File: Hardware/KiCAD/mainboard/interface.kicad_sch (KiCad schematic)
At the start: 22 parts, among them J2 USB_C, J3 UART, J4 Conn_01x30, J5 STLink, Q1 BSS138, U5 USBLC6-2

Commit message: Add files via upload
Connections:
- net BTN_F1: now also J4.18 (Pin_18)
- net GND: now also J4.10 (Pin_10), J4.26 (Pin_26), J4.28 (Pin_28)
- net VDD: now also J4.1 (Pin_1), J4.16 (Pin_16), J4.17 (Pin_17)
- net OLED_SPI_MOSI: now reaches J4.11 (Pin_11)
- net OLED_SPI_SCK: now reaches J4.12 (Pin_12)
- net OLED_CS: now reaches J4.13 (Pin_13)
- net OLED_DC: now reaches J4.14 (Pin_14)
- net OLED_RST: now reaches J4.15 (Pin_15)
- net BTN_F2: now reaches J4.19 (Pin_19)
- net C4: now reaches J4.2 (Pin_2)
- net PTT_IN: now reaches J4.20 (Pin_20)
- net ENC_A: now reaches J4.21 (Pin_21)
- net ENC_B: now reaches J4.22 (Pin_22)
- net ENC_BTN: now reaches J4.23 (Pin_23)
- net MIC_MUTE: now reaches J4.24 (Pin_24)
- net MIC_GAIN: now reaches J4.25 (Pin_25)
- net AUDIO_MIC: now reaches J4.27 (Pin_27)
- net SPK_P: now reaches J4.29 (Pin_29)
- net C3: now reaches J4.3 (Pin_3)
- net SPK_N: now reaches J4.30 (Pin_30)
- net C2: now reaches J4.4 (Pin_4)
- net C1: now reaches J4.5 (Pin_5)
- net R4: now reaches J4.6 (Pin_6)
- net R3: now reaches J4.7 (Pin_7)
- net R2: now reaches J4.8 (Pin_8)
- net R1: now reaches J4.9 (Pin_9)
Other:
- note removed: "TODO"
- moved on the sheet: J4

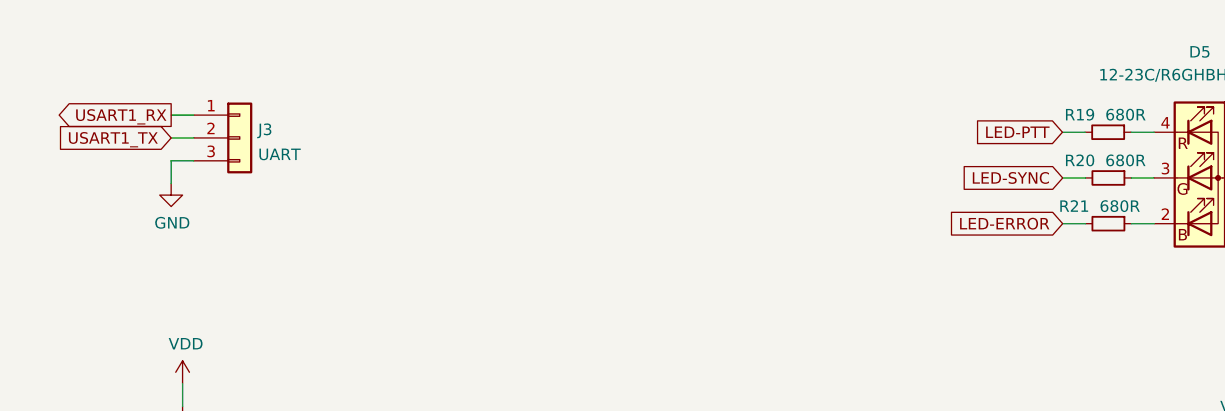
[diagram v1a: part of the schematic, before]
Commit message: J3 UART conn change
Fixes #33
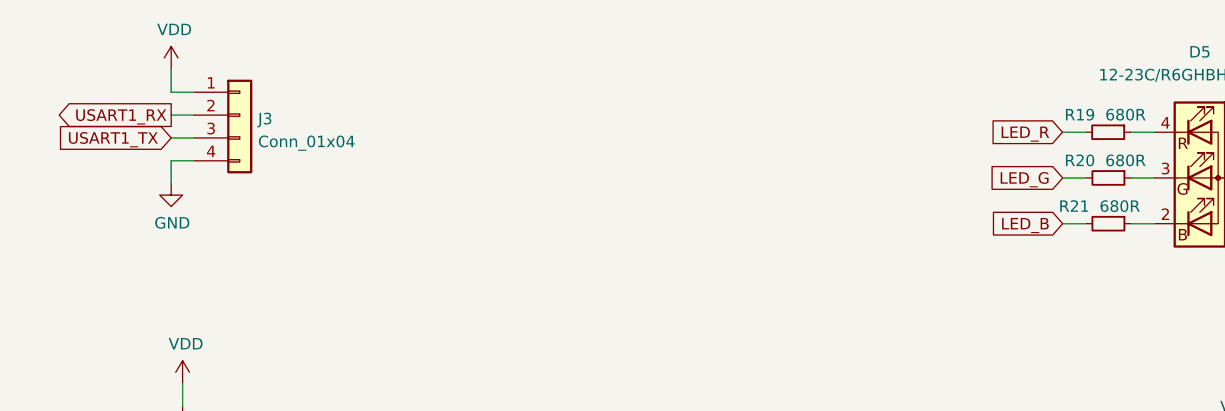
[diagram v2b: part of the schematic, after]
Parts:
- removed J3: UART, Connector_PinHeader_2.54mm:PinHeader_1x03_P2.54mm_Vertical, symbol Connector_Generic:Conn_01x03
- added J3: Conn_01x04, Connector_PinHeader_2.54mm:PinHeader_1x04_P2.54mm_Vertical, symbol Connector_Generic:Conn_01x04
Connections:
- net GND: now also J3.4 (Pin_4)
- net USART1_RX: now also J3.2 (Pin_2)
- net USART1_TX: now also J3.3 (Pin_3)
- net VDD: now also J3.1 (Pin_1)
- net LED-ERROR renamed LED_B
- net LED-PTT renamed LED_R
- net LED-SYNC renamed LED_G
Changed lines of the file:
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@@
+    (stroke (width 0) (type default) (color 0 0 0 0))
+  )
+  (wire (pts (xy 40.64 30.48) (xy 40.64 33.02))
     (stroke (width 0) (type default) (color 0 0 0 0))
   )
@@
   )
   (wire (pts (xy 161.29 97.79) (xy 161.29 138.43))
+    (stroke (width 0) (type default) (color 0 0 0 0))
+  )
+  (wire (pts (xy 40.64 33.02) (xy 43.18 33.02))
     (stroke (width 0) (type default) (color 0 0 0 0))
   )
@@
     )
   )
-  (global_label "LED-PTT" (shape input) (at 139.6709 37.465 180) (fields_autoplaced)
-    (effects (font (size 1.27 1.27)) (justify right))
-    (property "Intersheet References" "${INTERSHEET_REFS}" (id 0) (at -121.9491 -99.695 0)
-      (effects (font (size 1.27 1.27)) hide)
+  (global_label "LED_R" (shape input) (at 139.6709 37.465 180) (fields_autoplaced)
+    (effects (font (size 1.27 1.27)) (justify right))
+    (property "Intersheet References" "${INTERSHEET_REFS}" (id 0) (at 131.573 37.3856 0)
+      (effects (font (size 1.27 1.27)) (justify right) hide)
     )
   )
@@
     )
   )
-  (global_label "LED-SYNC" (shape input) (at 139.7 42.545 180) (fields_autoplaced)
-    (effects (font (size 1.27 1.27)) (justify right))
-    (property "Intersheet References" "${INTERSHEET_REFS}" (id 0) (at -121.92 -103.505 0)
-      (effects (font (size 1.27 1.27)) hide)
+  (global_label "LED_G" (shape input) (at 139.7 42.545 180) (fields_autoplaced)
+    (effects (font (size 1.27 1.27)) (justify right))
+    (property "Intersheet References" "${INTERSHEET_REFS}" (id 0) (at 131.6021 42.4656 0)
+      (effects (font (size 1.27 1.27)) (justify right) hide)
     )
   )
@@
     )
   )
-  (global_label "LED-ERROR" (shape input) (at 139.7 47.625 180) (fields_autoplaced)
-    (effects (font (size 1.27 1.27)) (justify right))
-    (property "Intersheet References" "${INTERSHEET_REFS}" (id 0) (at -121.92 -107.315 0)
-      (effects (font (size 1.27 1.27)) hide)
+  (global_label "LED_B" (shape input) (at 139.7 47.625 180) (fields_autoplaced)
+    (effects (font (size 1.27 1.27)) (justify right))
+    (property "Intersheet References" "${INTERSHEET_REFS}" (id 0) (at 131.6021 47.5456 0)
+      (effects (font (size 1.27 1.27)) (justify right) hide)
     )
   )
   (symbol (lib_id "power:VDD") (at 175.26 32.385 0) (unit 1)
     (in_bom yes) (on_board yes)
-    (property "Reference" "#PWR0105" (id 0) (at 175.26 36.195 0)
+    (property "Reference" "#PWR0108" (id 0) (at 175.26 36.195 0)
       (effects (font (size 1.27 1.27)) hide)
     )
@@
     (pin "6")
   )
+  (symbol (lib_id "Connector_Generic:Conn_01x04") (at 48.26 35.56 0) (unit 1)
+    (in_bom yes) (on_board yes) (fields_autoplaced)
+    (property "Reference" "J3" (id 0) (at 50.292 35.9953 0)
+      (effects (font (size 1.27 1.27)) (justify left))
+    )
+    (property "Value" "Conn_01x04" (id 1) (at 50.292 38.5322 0)
+      (effects (font (size 1.27 1.27)) (justify left))
+    )
+    (property "Footprint" "Connector_PinHeader_2.54mm:PinHeader_1x04_P2.54mm_Vertical" (id 2) (at 48.26 35.56 0)
+      (effects (font (size 1.27 1.27)) hide)
+    )
+    (property "Datasheet" "~" (id 3) (at 48.26 35.56 0)
+      (effects (font (size 1.27 1.27)) hide)
+    )
+    (pin "1")
+    (pin "2")
+    (pin "3")
+    (pin "4")
+  )
   (symbol (lib_id "Mainboard-rescue:BSS138-Transistor_FET") (at 39.37 83.185 0) (unit 1)
     (in_bom yes) (on_board yes)
@@
   (symbol (lib_id "power:+5V") (at 93.98 144.78 0) (unit 1)
     (in_bom yes) (on_board yes)
-    (property "Reference" "#PWR0103" (id 0) (at 93.98 148.59 0)
+    (property "Reference" "#PWR0104" (id 0) (at 93.98 148.59 0)
       (effects (font (size 1.27 1.27)) hide)
     )
@@
   (symbol (lib_id "power:GND") (at 64.77 146.05 90) (unit 1)
     (in_bom yes) (on_board yes)
-    (property "Reference" "#PWR0102" (id 0) (at 71.12 146.05 0)
+    (property "Reference" "#PWR0103" (id 0) (at 71.12 146.05 0)
       (effects (font (size 1.27 1.27)) hide)
     )
@@
   (symbol (lib_id "power:GND") (at 40.64 43.18 0) (unit 1)
     (in_bom yes) (on_board yes)
-    (property "Reference" "#PWR097" (id 0) (at 40.64 49.53 0)
+    (property "Reference" "#PWR098" (id 0) (at 40.64 49.53 0)
       (effects (font (size 1.27 1.27)) hide)
     )
@@
     (pin "2")
   )
+  (symbol (lib_id "power:VDD") (at 40.64 30.48 0) (unit 1)
+    (in_bom yes) (on_board yes)
+    (property "Reference" "#PWR097" (id 0) (at 40.64 34.29 0)
+      (effects (font (size 1.27 1.27)) hide)
+    )
+    (property "Value" "VDD" (id 1) (at 41.021 26.0858 0))
+    (property "Footprint" "" (id 2) (at 40.64 30.48 0)
+      (effects (font (size 1.27 1.27)) hide)
+    )
+    (property "Datasheet" "" (id 3) (at 40.64 30.48 0)
+      (effects (font (size 1.27 1.27)) hide)
+    )
+    (pin "1")
+  )
   (symbol (lib_id "pkl_device:pkl_R_Small") (at 144.7509 37.465 270) (unit 1)
     (in_bom yes) (on_board yes)
@@
   (symbol (lib_id "power:GND") (at 41.91 90.805 0) (unit 1)
     (in_bom yes) (on_board yes)
-    (property "Reference" "#PWR099" (id 0) (at 41.91 97.155 0)
+    (property "Reference" "#PWR0100" (id 0) (at 41.91 97.155 0)
       (effects (font (size 1.27 1.27)) hide)
     )
@@
   (symbol (lib_id "power:GND") (at 230.505 74.93 0) (unit 1)
     (in_bom yes) (on_board yes)
-    (property "Reference" "#PWR0108" (id 0) (at 230.505 81.28 0)
+    (property "Reference" "#PWR0111" (id 0) (at 230.505 81.28 0)
       (effects (font (size 1.27 1.27)) hide)
     )
@@
   (symbol (lib_id "power:GND") (at 161.29 151.13 0) (unit 1)
     (in_bom yes) (on_board yes)
-    (property "Reference" "#PWR?" (id 0) (at 161.29 157.48 0)
+    (property "Reference" "#PWR0106" (id 0) (at 161.29 157.48 0)
       (effects (font (size 1.27 1.27)) hide)
     )
@@
   (symbol (lib_id "power:GND") (at 238.76 45.72 0) (unit 1)
     (in_bom yes) (on_board yes)
-    (property "Reference" "#PWR0109" (id 0) (at 238.76 52.07 0)
+    (property "Reference" "#PWR0112" (id 0) (at 238.76 52.07 0)
       (effects (font (size 1.27 1.27)) hide)
     )
@@
   (symbol (lib_id "power:VDD") (at 230.505 57.15 0) (unit 1)
     (in_bom yes) (on_board yes)
-    (property "Reference" "#PWR0107" (id 0) (at 230.505 60.96 0)
+    (property "Reference" "#PWR0110" (id 0) (at 230.505 60.96 0)
       (effects (font (size 1.27 1.27)) hide)
     )
@@
   (symbol (lib_id "power:+5V") (at 64.77 137.16 0) (unit 1)
     (in_bom yes) (on_board yes)
-    (property "Reference" "#PWR0101" (id 0) (at 64.77 140.97 0)
+    (property "Reference" "#PWR0102" (id 0) (at 64.77 140.97 0)
       (effects (font (size 1.27 1.27)) hide)
     )
@@
   (symbol (lib_id "power:VDD") (at 162.56 39.37 0) (unit 1)
     (in_bom yes) (on_board yes)
-    (property "Reference" "#PWR0104" (id 0) (at 162.56 43.18 0)
+    (property "Reference" "#PWR0107" (id 0) (at 162.56 43.18 0)
       (effects (font (size 1.27 1.27)) hide)
     )
@@
   (symbol (lib_id "power:VDD") (at 41.91 65.405 0) (unit 1)
     (in_bom yes) (on_board yes)
-    (property "Reference" "#PWR098" (id 0) (at 41.91 69.215 0)
+    (property "Reference" "#PWR099" (id 0) (at 41.91 69.215 0)
       (effects (font (size 1.27 1.27)) hide)
     )
@@
   (symbol (lib_id "power:GND") (at 63.5 162.56 0) (unit 1)
     (in_bom yes) (on_board yes)
-    (property "Reference" "#PWR0100" (id 0) (at 63.5 168.91 0)
+    (property "Reference" "#PWR0101" (id 0) (at 63.5 168.91 0)
       (effects (font (size 1.27 1.27)) hide)
     )
@@
   (symbol (lib_id "power:GND") (at 175.26 46.99 0) (unit 1)
     (in_bom yes) (on_board yes)
-    (property "Reference" "#PWR0106" (id 0) (at 175.26 53.34 0)
+    (property "Reference" "#PWR0109" (id 0) (at 175.26 53.34 0)
       (effects (font (size 1.27 1.27)) hide)
     )
@@
     (pin "1")
   )
-  (symbol (lib_id "Connector_Generic:Conn_01x03") (at 48.26 38.1 0) (unit 1)
-    (in_bom yes) (on_board yes) (fields_autoplaced)
-    (property "Reference" "J3" (id 0) (at 50.2921 37.1915 0)
-      (effects (font (size 1.27 1.27)) (justify left))
-    )
-    (property "Value" "UART" (id 1) (at 50.2921 39.9666 0)
-      (effects (font (size 1.27 1.27)) (justify left))
-    )
-    (property "Footprint" "Connector_PinHeader_2.54mm:PinHeader_1x03_P2.54mm_Vertical" (id 2) (at 48.26 38.1 0)
-      (effects (font (size 1.27 1.27)) hide)
-    )
-    (property "Datasheet" "~" (id 3) (at 48.26 38.1 0)
-      (effects (font (size 1.27 1.27)) hide)
-    )
-    (pin "1")
-    (pin "2")
-    (pin "3")
-  )
   (symbol (lib_id "power:VDD") (at 158.75 72.39 0) (unit 1)
     (in_bom yes) (on_board yes)
-    (property "Reference" "#PWR?" (id 0) (at 158.75 76.2 0)
-      (effects (font (size 1.27 1.27)) hide)
-    )
+    (property "Reference" "#PWR0105" (id 0) (at 158.75 76.2 0)
+      (effects (font (size 1.27 1.27)) hide)
+    )

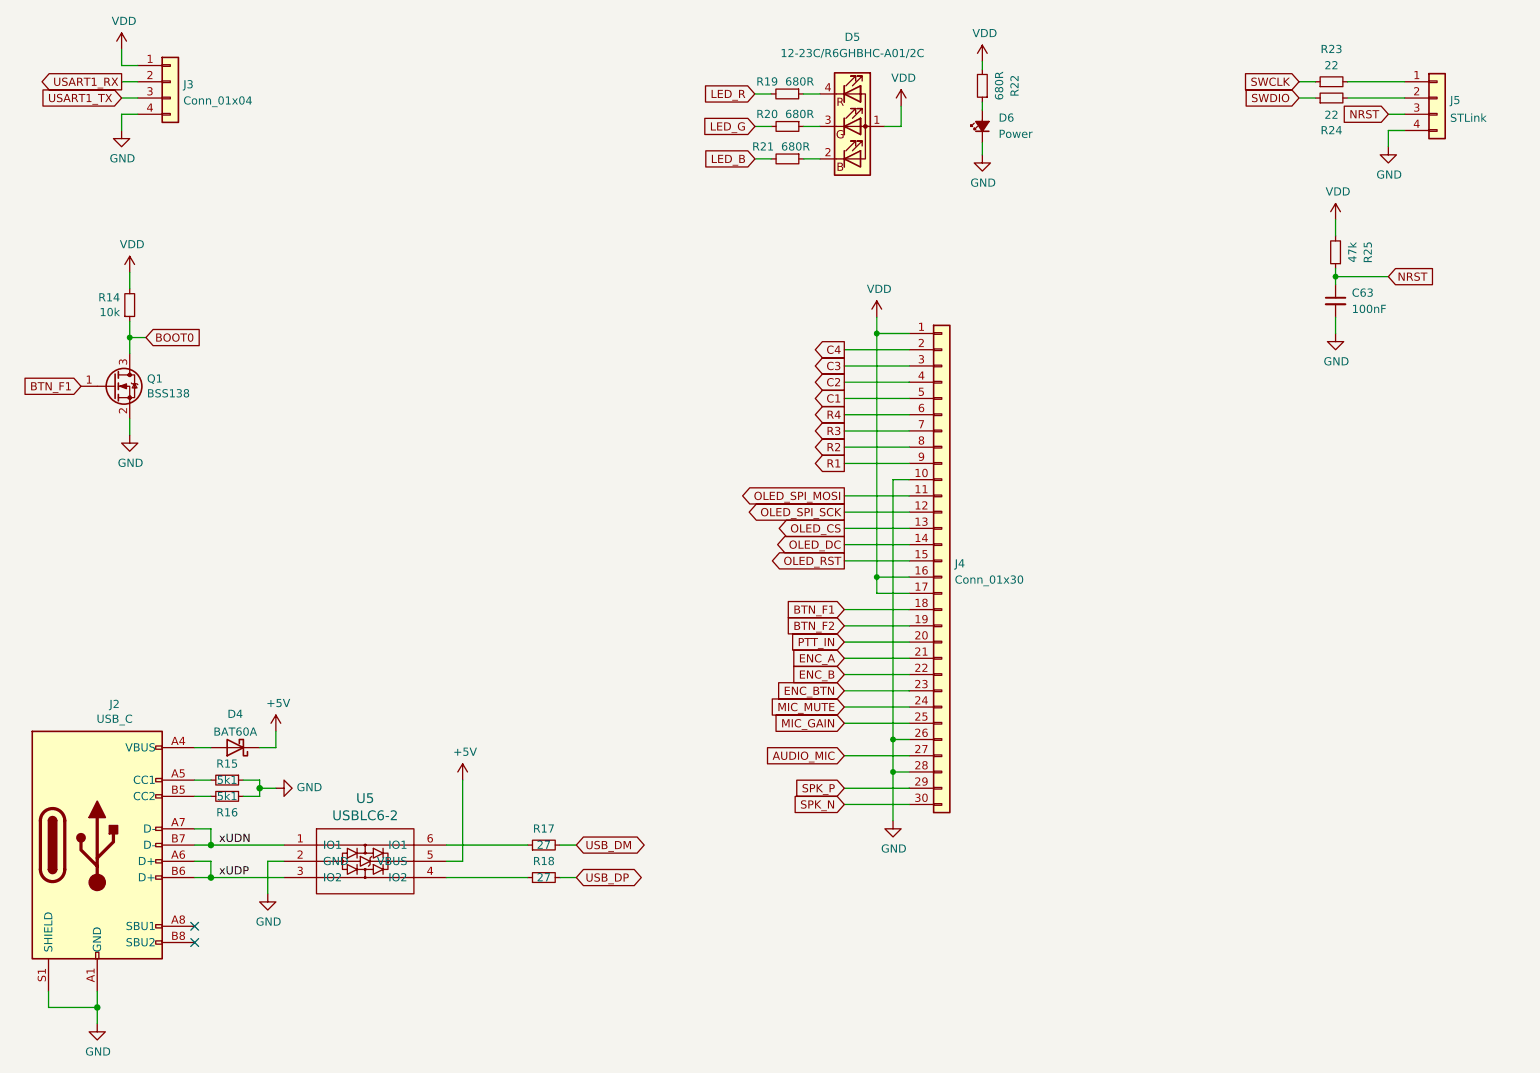
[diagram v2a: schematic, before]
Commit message: MCU swap
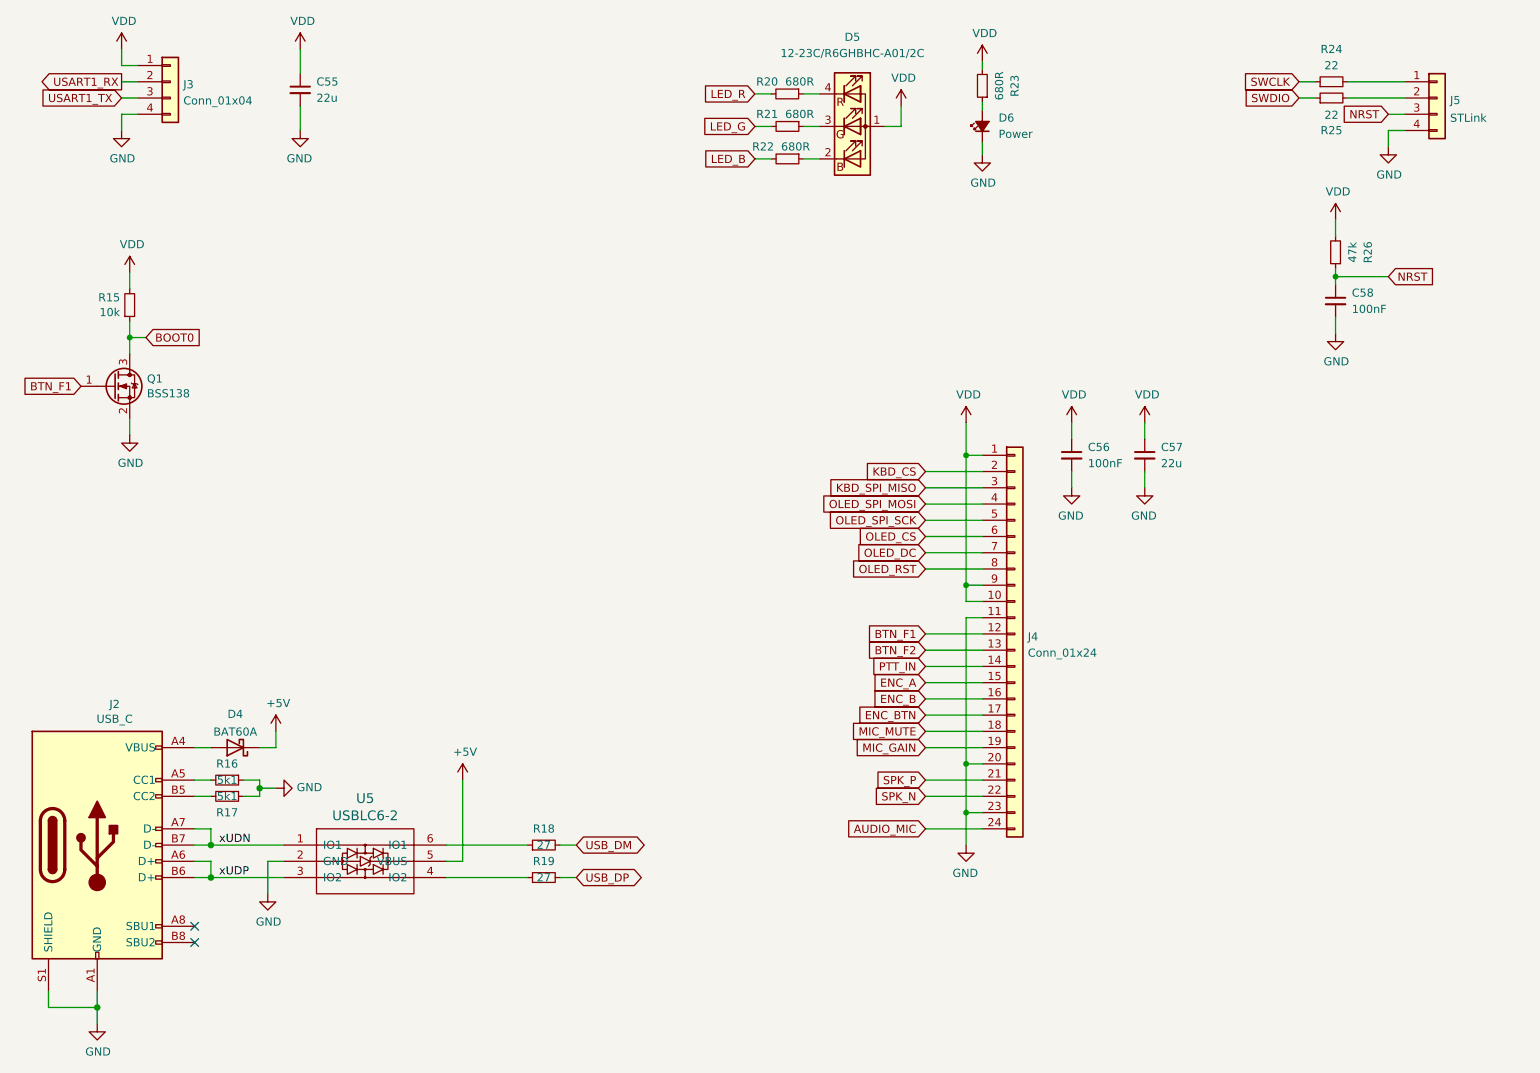
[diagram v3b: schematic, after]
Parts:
- removed J4: Conn_01x30, symbol Connector_Generic:Conn_01x30
- added C55, C57: 22u, Capacitor_SMD:C_1210_3225Metric, symbol pkl_device:pkl_C_Small
- added C56: 100nF, Capacitor_SMD:C_0402_1005Metric, symbol Device:C_Small
- added J4: Conn_01x24, symbol Connector_Generic:Conn_01x24
- renumbered C63 to C58, R14 to R15, R15 to R16, R16 to R17, R17 to R18, R18 to R19, R19 to R20, R20 to R21, R21 to R22, R22 to R23, R23 to R24, R24 to R25, R25 to R26
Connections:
- net AUDIO_MIC: now also J4.24 (Pin_24)
- net BTN_F1: now also J4.12 (Pin_12)
- net BTN_F2: now also J4.13 (Pin_13)
- net ENC_A: now also J4.15 (Pin_15)
- net ENC_B: now also J4.16 (Pin_16)
- net ENC_BTN: now also J4.17 (Pin_17)
- net GND: now also C55.2, C56.2, C57.2, J4.11 (Pin_11), J4.20 (Pin_20), J4.23 (Pin_23)
- net MIC_GAIN: now also J4.19 (Pin_19)
- net MIC_MUTE: now also J4.18 (Pin_18)
- net OLED_CS: now also J4.6 (Pin_6)
- net OLED_DC: now also J4.7 (Pin_7)
- net OLED_RST: now also J4.8 (Pin_8)
- net OLED_SPI_MOSI: now also J4.4 (Pin_4)
- net OLED_SPI_SCK: now also J4.5 (Pin_5)
- net PTT_IN: now also J4.14 (Pin_14)
- net SPK_N: now also J4.22 (Pin_22)
- net SPK_P: now also J4.21 (Pin_21)
- net VDD: now also C55.1, C56.1, C57.1, J4.1 (Pin_1), J4.10 (Pin_10), J4.9 (Pin_9)
- new net KBD_CS: J4.2 (Pin_2)
- new net KBD_SPI_MISO: J4.3 (Pin_3)
